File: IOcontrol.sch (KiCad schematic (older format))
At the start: 7 parts, among them P301 On Switch, P302 Vcc, P303 PowerGND, P304 RegulatedPWR, P305 RegulatedGND

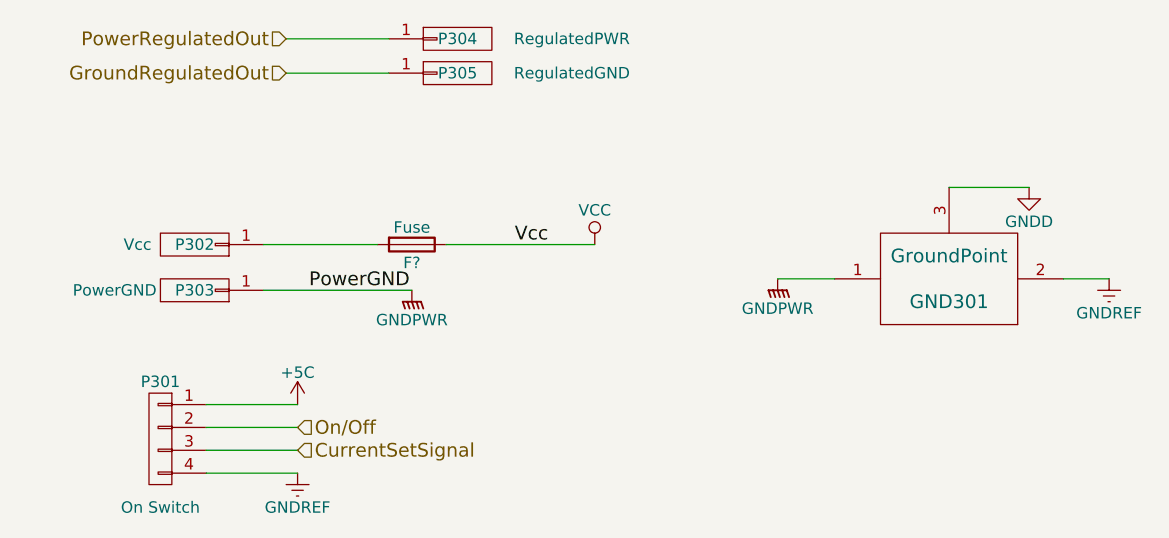
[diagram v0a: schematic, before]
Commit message: Resolved library issues
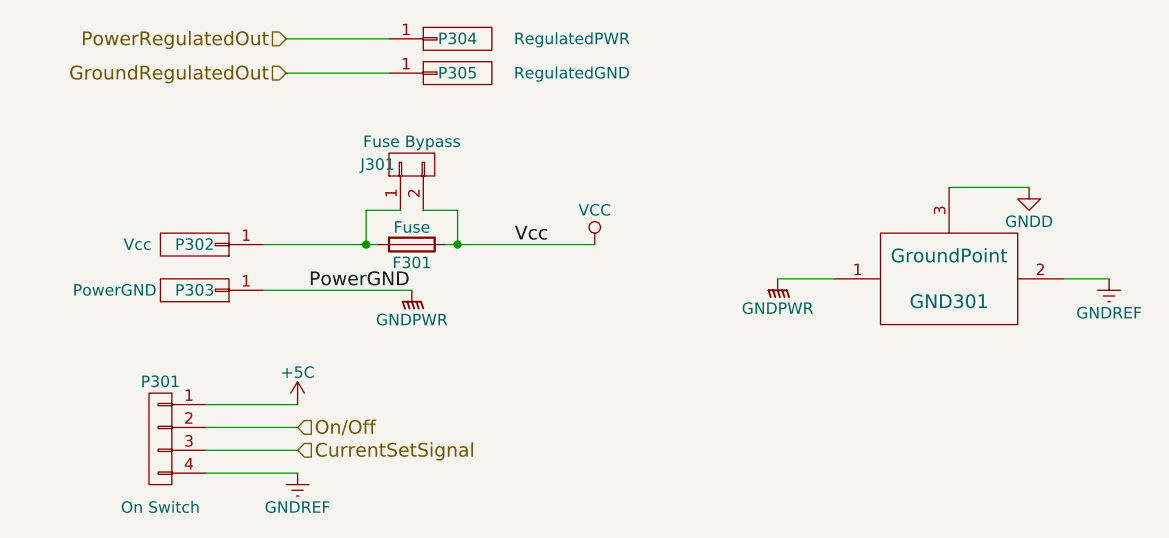
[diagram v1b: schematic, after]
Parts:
- added J301: Fuse Bypass, Pin_Headers:Pin_Header_Angled_1x02_Pitch2.54mm, symbol CONN_01X02
- F301: renamed from F?; footprint (none) -> axel:Littlefuse-holder
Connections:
- net VCC: now also J301.2 (P2)
- net at F301.2, P302.1 (P1): now also J301.1 (P1)
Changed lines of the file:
@@
 EESchema Schematic File Version 2
+LIBS:sjaxel
+LIBS:74xgxx
+LIBS:74xx
+LIBS:ac-dc
+LIBS:actel
+LIBS:adc-dac
+LIBS:allegro
+LIBS:Altera
+LIBS:analog_devices
+LIBS:analog_switches
+LIBS:atmel
+LIBS:audio
+LIBS:battery_management
+LIBS:bbd
+LIBS:bosch
+LIBS:brooktre
+LIBS:cmos4000
+LIBS:cmos_ieee
+LIBS:conn
+LIBS:contrib
+LIBS:cypress
+LIBS:dc-dc
+LIBS:device
+LIBS:digital-audio
+LIBS:diode
+LIBS:display
+LIBS:dsp
+LIBS:elec-unifil
+LIBS:ESD_Protection
+LIBS:ftdi
+LIBS:gennum
+LIBS:graphic
+LIBS:hc11
+LIBS:intel
+LIBS:interface
+LIBS:ir
+LIBS:Lattice
+LIBS:leds
+LIBS:linear
+LIBS:logo
+LIBS:maxim
+LIBS:mechanical
+LIBS:memory
+LIBS:microchip
+LIBS:microchip_dspic33dsc
+LIBS:microchip_pic10mcu
+LIBS:microchip_pic12mcu
+LIBS:microchip_pic16mcu
+LIBS:microchip_pic18mcu
+LIBS:microchip_pic24mcu
+LIBS:microchip_pic32mcu
+LIBS:microcontrollers
+LIBS:modules
+LIBS:motor_drivers
+LIBS:motorola
+LIBS:motors
+LIBS:msp430
+LIBS:nordicsemi
+LIBS:nxp
+LIBS:nxp_armmcu
+LIBS:onsemi
+LIBS:opto
+LIBS:Oscillators
+LIBS:philips
 LIBS:power
-LIBS:device
+LIBS:powerint
+LIBS:Power_Management
+LIBS:pspice
+LIBS:references
+LIBS:regul
+LIBS:relays
+LIBS:rfcom
+LIBS:sensors
+LIBS:silabs
+LIBS:siliconi
+LIBS:stm8
+LIBS:stm32
+LIBS:supertex
+LIBS:switches
+LIBS:texas
+LIBS:transf
 LIBS:transistors
-LIBS:conn
-LIBS:linear
-LIBS:regul
-LIBS:74xx
-LIBS:cmos4000
-LIBS:adc-dac
-LIBS:memory
+LIBS:triac_thyristor
+LIBS:ttl_ieee
+LIBS:valves
+LIBS:video
+LIBS:wiznet
+LIBS:Worldsemi
+LIBS:Xicor
 LIBS:xilinx
-LIBS:microcontrollers
-LIBS:dsp
-LIBS:microchip
-LIBS:analog_switches
-LIBS:motorola
-LIBS:texas
-LIBS:intel
-LIBS:audio
-LIBS:interface
-LIBS:digital-audio
-LIBS:philips
-LIBS:display
-LIBS:cypress
-LIBS:siliconi
-LIBS:opto
-LIBS:atmel
-LIBS:contrib
-LIBS:valves
-LIBS:sjaxel
+LIBS:zetex
+LIBS:Zilog
+LIBS:driver-boostcon-cache
 EELAYER 25 0
 EELAYER END
@@
 	2600 2050 3250 2050
 $Comp
-L Fuse F?
+L Fuse F301
 U 1 1 58FAAAA5
 P 2450 2050
-F 0 "F?" V 2530 2050 50  0000 C CNN
+F 0 "F301" V 2530 2050 50  0000 C CNN
 F 1 "Fuse" V 2375 2050 50  0000 C CNN
-F 2 "" V 2380 2050 50  0001 C CNN
+F 2 "axel:Littlefuse-holder" V 2380 2050 50  0001 C CNN
 F 3 "" H 2450 2050 50  0001 C CNN
 	1    2450 2050
 	0    1    1    0
 $EndComp
+$Comp
+L CONN_01X02 J301
+U 1 1 58FC07DF
+P 2450 1700
+F 0 "J301" V 2450 1850 50  0000 C CNN
+F 1 "Fuse Bypass" V 2550 1700 50  0000 C CNN
+F 2 "Pin_Headers:Pin_Header_Angled_1x02_Pitch2.54mm" H 2450 1700 50  0001 C CNN
+F 3 "" H 2450 1700 50  0001 C CNN
+	1    2450 1700
+	0    -1   -1   0
+$EndComp
+Wire Wire Line
+	2250 2050 2250 1900
+Wire Wire Line
+	2250 1900 2400 1900
+Connection ~ 2250 2050
+Wire Wire Line
+	2500 1900 2650 1900
+Wire Wire Line
+	2650 1900 2650 2050
+Connection ~ 2650 2050
 $EndSCHEMATC

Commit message: Syncing
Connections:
- net GNDPWR: now also GND301.2; no longer GND301.1
- net GNDREF: now also GND301.1; no longer GND301.2
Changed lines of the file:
@@
 L GNDPWR #PWR08
 U 1 1 58F8EFB4
-P 4050 2200
-F 0 "#PWR08" H 4050 2000 50  0001 C CNN
-F 1 "GNDPWR" H 4050 2070 50  0000 C CNN
-F 2 "" H 4050 2150 50  0000 C CNN
-F 3 "" H 4050 2150 50  0000 C CNN
-	1    4050 2200
+P 5500 2200
+F 0 "#PWR08" H 5500 2000 50  0001 C CNN
+F 1 "GNDPWR" H 5500 2050 50  0000 C CNN
+F 2 "" H 5500 2150 50  0000 C CNN
+F 3 "" H 5500 2150 50  0000 C CNN
+	1    5500 2200
 	-1   0    0    -1
 $EndComp
@@
 L GNDREF #PWR09
 U 1 1 58F8F058
-P 5500 2200
-F 0 "#PWR09" H 5500 1950 50  0001 C CNN
-F 1 "GNDREF" H 5500 2050 50  0000 C CNN
-F 2 "" H 5500 2200 50  0000 C CNN
-F 3 "" H 5500 2200 50  0000 C CNN
-	1    5500 2200
+P 4050 2200
+F 0 "#PWR09" H 4050 1950 50  0001 C CNN
+F 1 "GNDREF" H 4050 2050 50  0000 C CNN
+F 2 "" H 4050 2200 50  0000 C CNN
+F 3 "" H 4050 2200 50  0000 C CNN
+	1    4050 2200
 	1    0    0    -1
 $EndComp

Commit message: New amplifiers, fuse and general mayhem
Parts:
- removed P305: RegulatedGND, Mounting_Holes:MountingHole_3.2mm_M3_Pad, symbol PowerConnector_01x01
- F301: footprint axel:Littlefuse-holder -> axel:Littlefuse_30mm_M5
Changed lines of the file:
@@
 Wire Wire Line
 	1900 1150 2350 1150
-Text HLabel 1900 1300 0    60   Input ~ 0
-GroundRegulatedOut
-Wire Wire Line
-	1900 1300 2350 1300
 Wire Wire Line
 	1800 2250 2450 2250
@@
 F 3 "" H 2550 1150 50  0000 C CNN
 	1    2600 1150
-	1    0    0    -1
-$EndComp
-$Comp
-L PowerConnector_01x01 P305
-U 1 1 58F16725
-P 2600 1300
-F 0 "P305" H 2650 1300 50  0000 C CNN
-F 1 "RegulatedGND" H 3150 1300 50  0000 C CNN
-F 2 "Mounting_Holes:MountingHole_3.2mm_M3_Pad" H 2550 1300 50  0001 C CNN
-F 3 "" H 2550 1300 50  0000 C CNN
-	1    2600 1300
 	1    0    0    -1
 $EndComp
@@
 F 0 "F301" V 2530 2050 50  0000 C CNN
 F 1 "Fuse" V 2375 2050 50  0000 C CNN
-F 2 "axel:Littlefuse-holder" V 2380 2050 50  0001 C CNN
+F 2 "axel:Littlefuse_30mm_M5" V 2380 2050 50  0001 C CNN
 F 3 "" H 2450 2050 50  0001 C CNN
 	1    2450 2050
